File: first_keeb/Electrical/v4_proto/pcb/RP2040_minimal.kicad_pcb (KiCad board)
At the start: 2 copper layers, 80 x 80 mm, 64 parts, among them P1 USB4105-GF-A, Q1 SN74LV1T34DBV, SW1 SW_Push, SW2 SW_Push, SW3 SKRKAGE020, U1 NCP1117-3.3_SOT223, U2 LM4040DBZ-3, U3 PRTR5V0U2X, U4 W25Q32JVSS, U5 RP2040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

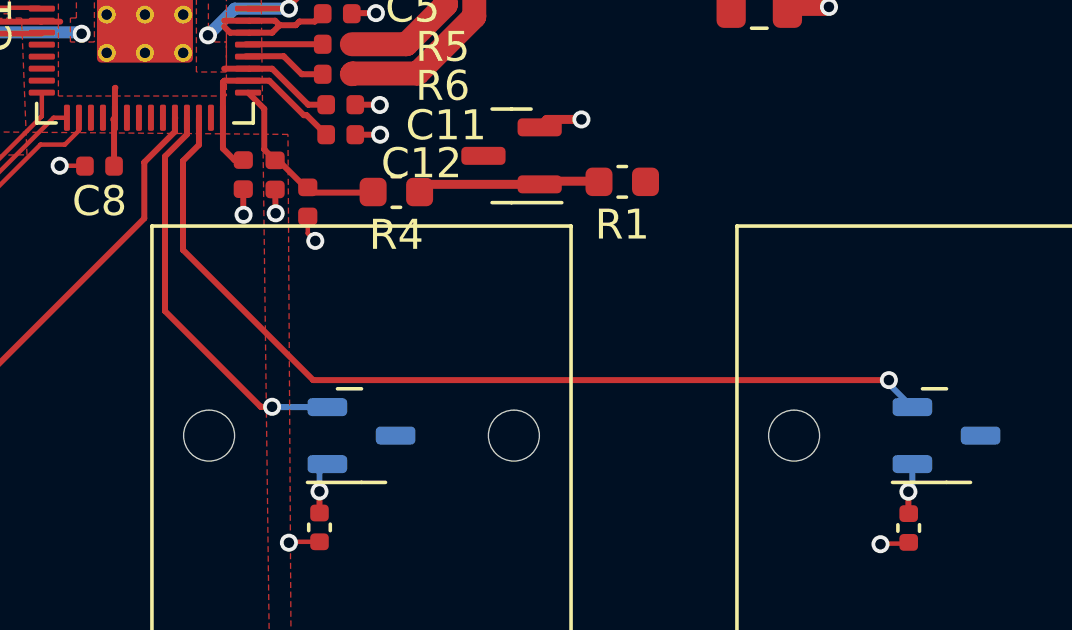
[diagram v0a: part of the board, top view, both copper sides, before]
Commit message: removes extra led
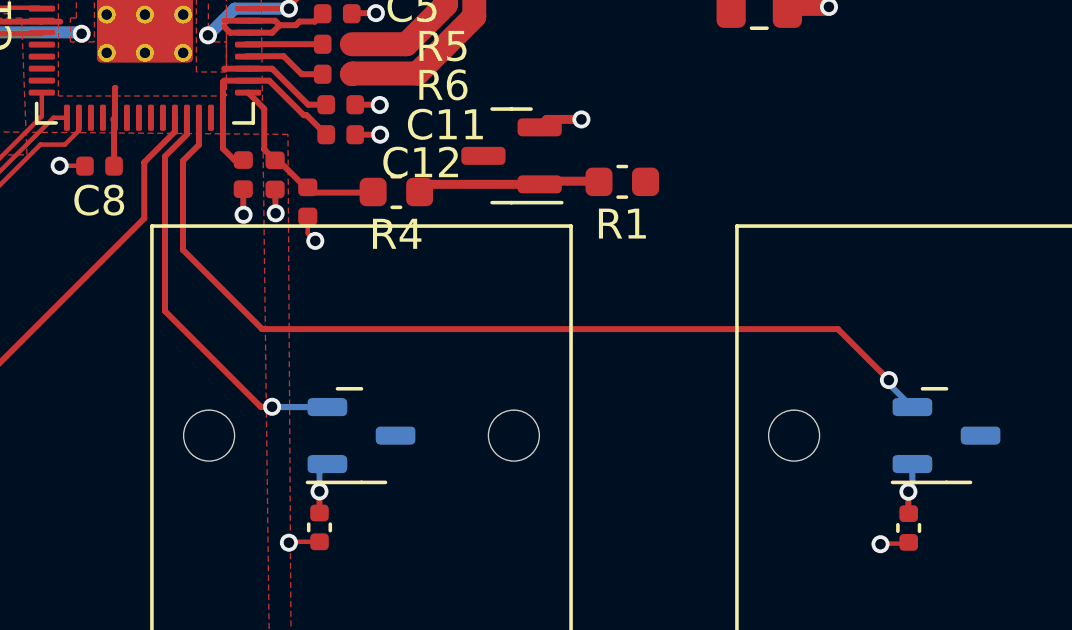
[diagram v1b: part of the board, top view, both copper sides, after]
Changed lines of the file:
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@@
   (segment (start 97.11 99.05) (end 98.8625 99.05) (width 0.2) (layer "B.Cu") (net 46))
   (segment (start 97.02 99.04) (end 97.11 99.05) (width 0.2) (layer "B.Cu") (net 46))
+  (segment (start 96.69 96.45) (end 94.05 93.81) (width 0.2) (layer "F.Cu") (net 47))
   (segment (start 94.579338 89.4075) (end 94.581838 89.405) (width 0.2) (layer "F.Cu") (net 47))
-  (segment (start 98.39 98.15) (end 94.05 93.81) (width 0.2) (layer "F.Cu") (net 47))
+  (segment (start 115.88 96.45) (end 96.69 96.45) (width 0.2) (layer "F.Cu") (net 47))
+  (segment (start 94.581838 90.308162) (end 94.581838 89.405) (width 0.2) (layer "F.Cu") (net 47))
   (segment (start 94.05 90.84) (end 94.581838 90.308162) (width 0.2) (layer "F.Cu") (net 47))
   (segment (start 94.05 93.81) (end 94.05 90.84) (width 0.2) (layer "F.Cu") (net 47))
-  (segment (start 117.58 98.15) (end 98.39 98.15) (width 0.2) (layer "F.Cu") (net 47))
-  (segment (start 94.581838 90.308162) (end 94.581838 89.405) (width 0.2) (layer "F.Cu") (net 47))
+  (segment (start 117.58 98.15) (end 115.88 96.45) (width 0.2) (layer "F.Cu") (net 47))
   (via (at 117.58 98.15) (size 0.6) (drill 0.35) (layers "F.Cu" "B.Cu") (net 47))
   (segment (start 117.58 98.28) (end 117.58 98.15) (width 0.15) (layer "B.Cu") (net 47))

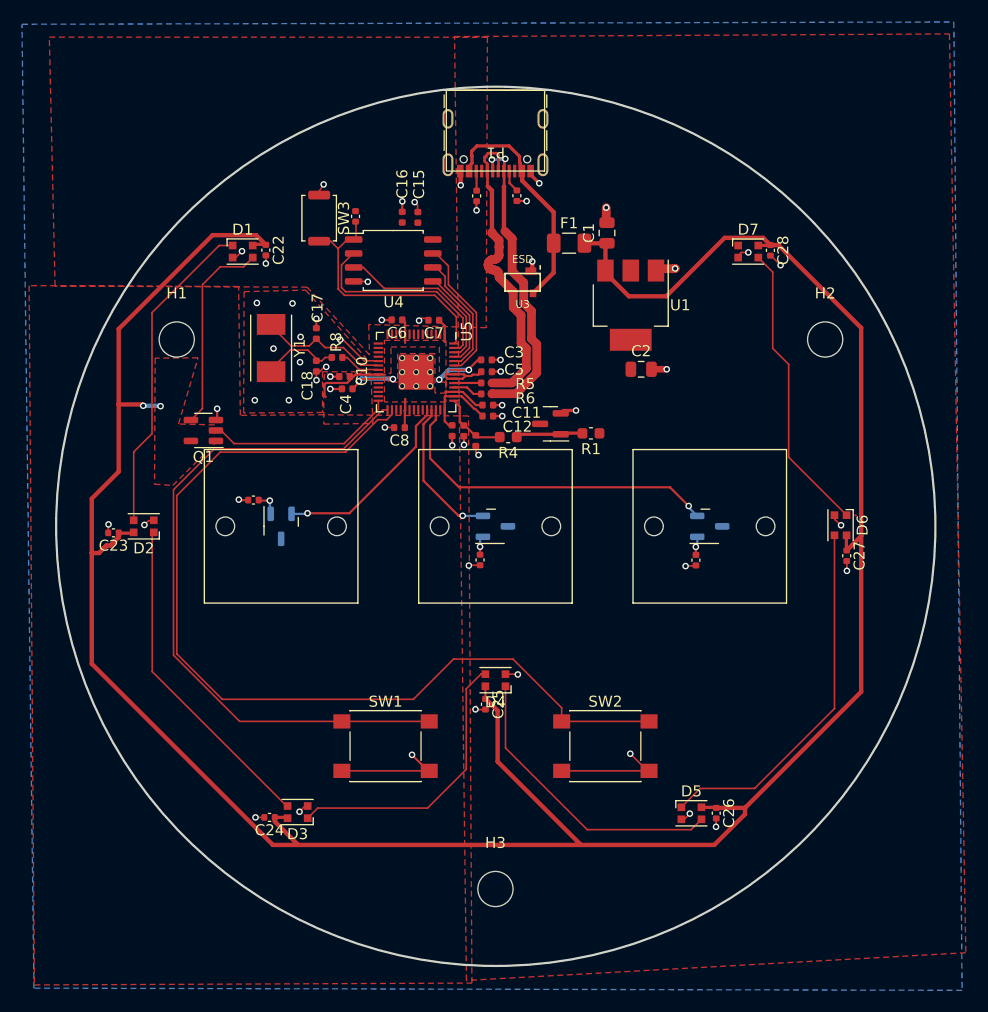
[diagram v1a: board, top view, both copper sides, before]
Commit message: makes 3v3 pour have more access
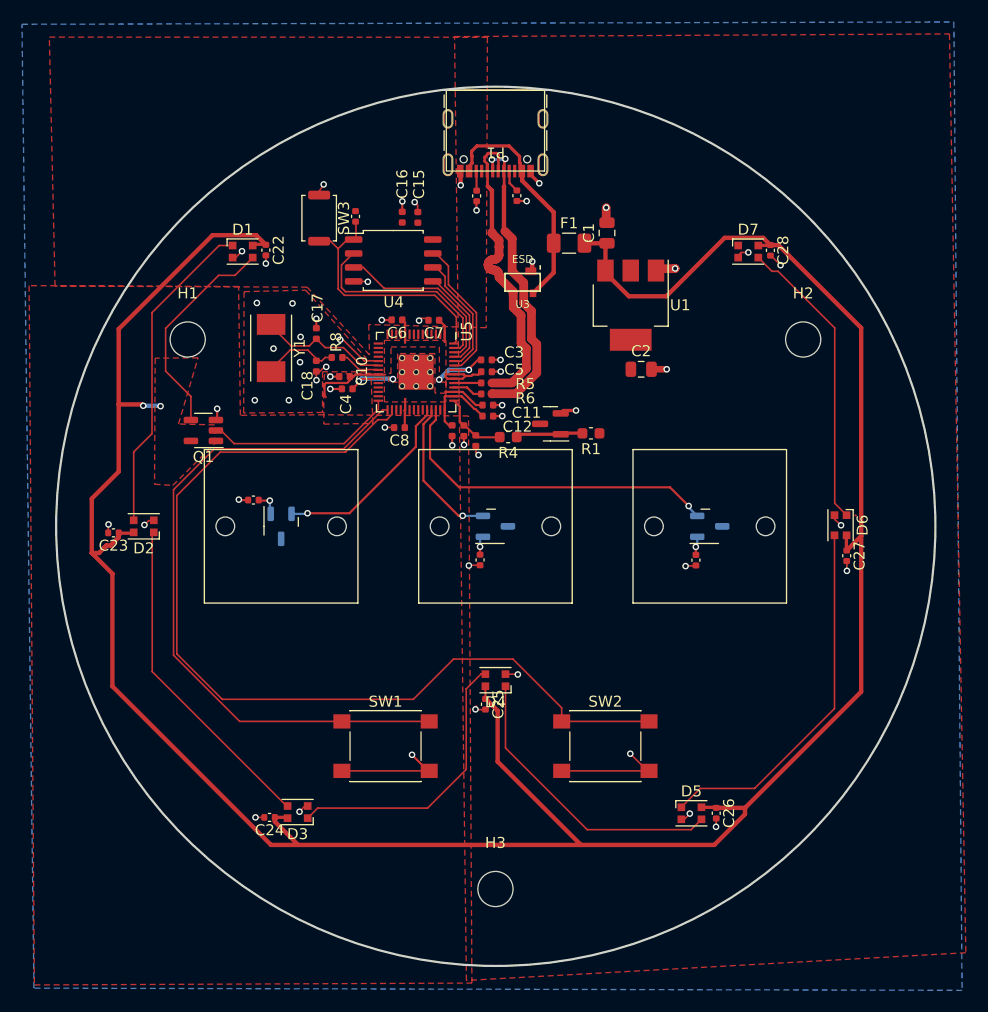
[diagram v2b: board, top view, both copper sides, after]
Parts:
- moved H2 2.00 mm to (128.0, 83.0)
- moved H1 1.00 mm to (72.0, 83.0)
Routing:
- net LED_D_5V: track 18.3 -> 19.9 mm
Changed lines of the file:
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@@
   )
   (footprint "MountingHole:MountingHole_3.2mm_M3" (layer "F.Cu")
-    (at 130 83)
+    (at 128 83)
     (descr "Mounting Hole 3.2mm, no annular, M3")
     (tags "mounting hole 3.2mm no annular m3")
@@
   )
   (footprint "MountingHole:MountingHole_3.2mm_M3" (layer "F.Cu")
-    (at 71 83)
+    (at 72 83)
     (descr "Mounting Hole 3.2mm, no annular, M3")
     (tags "mounting hole 3.2mm no annular m3")
@@
     )
   )
+  (gr_circle (center 100 100) (end 136 100)
+    (stroke (width 0.1) (type default)) (fill none) (layer "Cmts.User"))
   (gr_circle (center 100.029338 100) (end 60.029338 100)
     (stroke (width 0.2) (type default)) (fill none) (layer "Edge.Cuts"))
@@
   (segment (start 87.556838 86.8025) (end 87.799338 86.56) (width 0.4) (layer "B.Cu") (net 6))
   (segment (start 87.799338 86.56) (end 90.614368 86.56) (width 0.4) (layer "B.Cu") (net 6))
-  (segment (start 126.68 93.715) (end 126.68 85.26) (width 0.15) (layer "F.Cu") (net 10))
-  (segment (start 125.23 83.81) (end 125.23 76.865) (width 0.15) (layer "F.Cu") (net 10))
-  (segment (start 131.95 98.985) (end 126.68 93.715) (width 0.15) (layer "F.Cu") (net 10))
-  (segment (start 125.23 76.865) (end 123.915 75.55) (width 0.15) (layer "F.Cu") (net 10))
-  (segment (start 126.68 85.26) (end 125.23 83.81) (width 0.15) (layer "F.Cu") (net 10))
+  (segment (start 131.95 98.985) (end 130.87 97.905) (width 0.15) (layer "F.Cu") (net 10))
+  (segment (start 125.1625 76.7975) (end 123.915 75.55) (width 0.15) (layer "F.Cu") (net 10))
+  (segment (start 125.7175 76.7975) (end 125.1625 76.7975) (width 0.15) (layer "F.Cu") (net 10))
+  (segment (start 130.87 81.95) (end 125.7175 76.7975) (width 0.15) (layer "F.Cu") (net 10))
+  (segment (start 130.87 97.905) (end 130.87 81.95) (width 0.15) (layer "F.Cu") (net 10))
   (segment (start 132.82 99.03) (end 132.73 98.98) (width 0.15) (layer "F.Cu") (net 10))
   (segment (start 96.219338 83.3675) (end 96.439338 83.1475) (width 0.15) (layer "F.Cu") (net 18))
@@
   (segment (start 83.704319 84.9385) (end 83.704319 84.741) (width 0.15) (layer "F.Cu") (net 33))
   (segment (start 82.933319 83.97) (end 81.320356 83.97) (width 0.15) (layer "F.Cu") (net 33))
-  (segment (start 77.075 76.39) (end 77.915 75.55) (width 0.15) (layer "F.Cu") (net 37))
-  (segment (start 73.34 78.01) (end 74.96 76.39) (width 0.15) (layer "F.Cu") (net 37))
-  (segment (start 73.34 89.281838) (end 73.34 78.01) (width 0.15) (layer "F.Cu") (net 37))
-  (segment (start 72.291838 90.33) (end 73.34 89.281838) (width 0.15) (layer "F.Cu") (net 37))
-  (segment (start 74.96 76.39) (end 77.075 76.39) (width 0.15) (layer "F.Cu") (net 37))
+  (segment (start 74.815 77.165) (end 76.3 77.165) (width 0.15) (layer "F.Cu") (net 37))
+  (segment (start 69.99 85.88) (end 69.99 81.99) (width 0.15) (layer "F.Cu") (net 37))
+  (segment (start 72.291838 90.33) (end 72.291838 88.181838) (width 0.15) (layer "F.Cu") (net 37))
+  (segment (start 69.99 81.99) (end 74.815 77.165) (width 0.15) (layer "F.Cu") (net 37))
+  (segment (start 76.3 77.165) (end 77.915 75.55) (width 0.15) (layer "F.Cu") (net 37))
+  (segment (start 72.291838 88.181838) (end 69.99 85.88) (width 0.15) (layer "F.Cu") (net 37))
   (segment (start 77.915 74.45) (end 78.025 74.34) (width 0.3) (layer "F.Cu") (net 38))
   (segment (start 108.131838 74.2475) (end 110.149338 74.2475) (width 0.4) (layer "F.Cu") (net 38))
@@
   (segment (start 133.27701 81.941989) (end 133.27701 100.88299) (width 0.4) (layer "F.Cu") (net 38))
   (segment (start 65.72 88.91) (end 65.72 82.05) (width 0.4) (layer "F.Cu") (net 38))
+  (segment (start 65.15 114.56) (end 65.15 104.31) (width 0.4) (layer "F.Cu") (net 38))
   (segment (start 124.36 73.75) (end 120.86 73.75) (width 0.4) (layer "F.Cu") (net 38))
   (segment (start 63.27 102.43) (end 63.932964 102.43) (width 0.4) (layer "F.Cu") (net 38))
@@
   (segment (start 82.05 128.99) (end 79.9275 126.8675) (width 0.4) (layer "F.Cu") (net 38))
   (segment (start 99.085 114.55) (end 99.085 115.705) (width 0.2) (layer "F.Cu") (net 38))
-  (segment (start 63.27 112.506739) (end 63.27 102.43) (width 0.4) (layer "F.Cu") (net 38))
   (segment (start 67.83 88.91) (end 67.95 89.03) (width 0.4) (layer "F.Cu") (net 38))
   (segment (start 99.085 115.705) (end 99.09 115.71) (width 0.2) (layer "F.Cu") (net 38))
   (segment (start 81.22 126.48) (end 79.885 126.48) (width 0.3) (layer "F.Cu") (net 38))
   (segment (start 65.72 82.05) (end 74.26 73.51) (width 0.4) (layer "F.Cu") (net 38))
+  (segment (start 65.15 104.31) (end 63.27 102.43) (width 0.4) (layer "F.Cu") (net 38))
   (segment (start 99.132965 115.71) (end 99.09 115.71) (width 0.4) (layer "F.Cu") (net 38))
   (segment (start 110.360588 74.24) (end 110.01 74.590588) (width 0.4) (layer "F.Cu") (net 38))
   (segment (start 78.025 74.34) (end 79.255 74.34) (width 0.3) (layer "F.Cu") (net 38))
   (segment (start 107.78 128.99) (end 82.05 128.99) (width 0.4) (layer "F.Cu") (net 38))
-  (segment (start 82.05 128.99) (end 79.753261 128.99) (width 0.4) (layer "F.Cu") (net 38))
   (segment (start 67.06 100.625) (end 65.725 100.625) (width 0.3) (layer "F.Cu") (net 38))
-  (segment (start 79.753261 128.99) (end 63.27 112.506739) (width 0.4) (layer "F.Cu") (net 38))
   (segment (start 63.932964 102.43) (end 64.621482 101.741482) (width 0.4) (layer "F.Cu") (net 38))
   (segment (start 122.709239 125.62) (end 122.709239 126.190761) (width 0.4) (layer "F.Cu") (net 38))
@@
   (segment (start 110.01 74.590588) (end 110.01 76.73) (width 0.4) (layer "F.Cu") (net 38))
   (segment (start 112.139706 79.07) (end 110 76.930294) (width 0.4) (layer "F.Cu") (net 38))
+  (segment (start 79.58 128.99) (end 65.15 114.56) (width 0.4) (layer "F.Cu") (net 38))
   (segment (start 65.72 88.91) (end 67.83 88.91) (width 0.4) (layer "F.Cu") (net 38))
   (segment (start 115.54 79.07) (end 112.139706 79.07) (width 0.4) (layer "F.Cu") (net 38))
+  (segment (start 82.05 128.99) (end 79.58 128.99) (width 0.4) (layer "F.Cu") (net 38))
   (segment (start 133.27701 100.88299) (end 131.96 102.2) (width 0.4) (layer "F.Cu") (net 38))
   (segment (start 108.024338 74.355) (end 108.131838 74.2475) (width 0.4) (layer "F.Cu") (net 38))

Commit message: first prototype of case
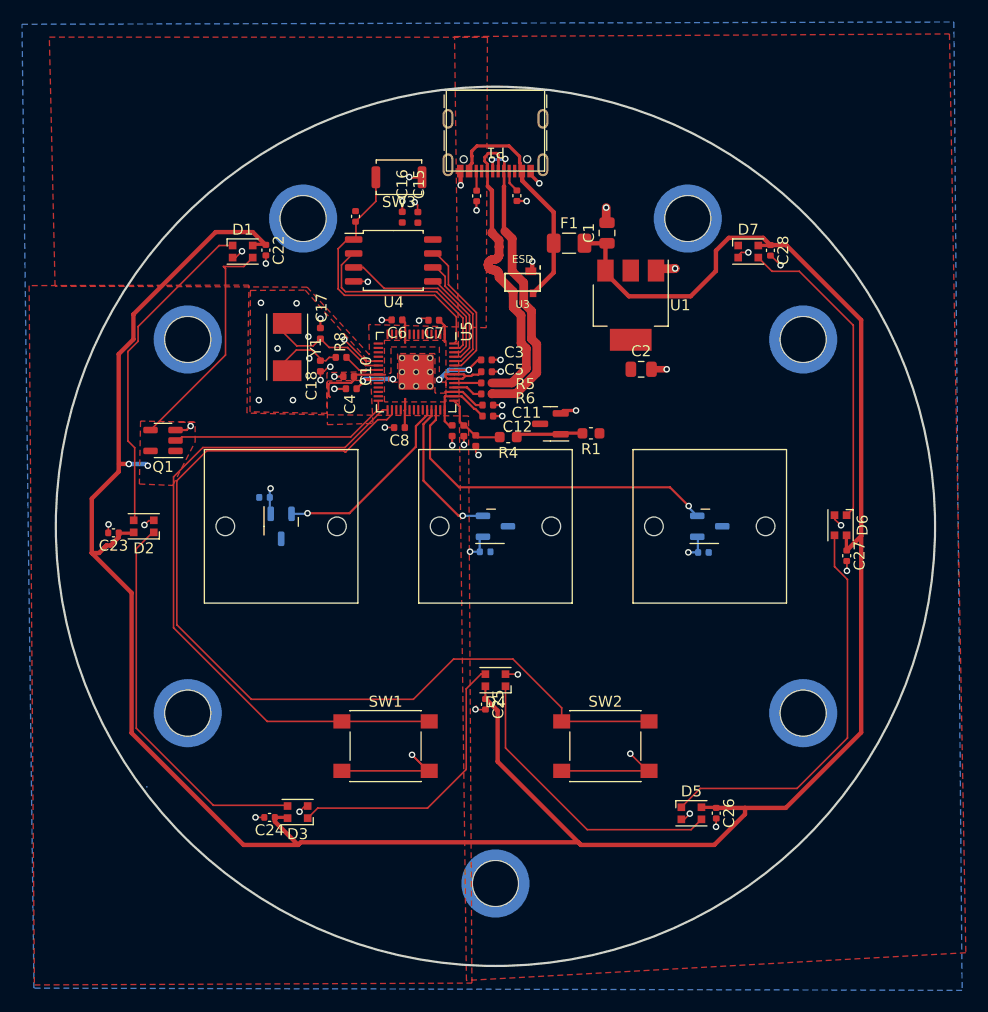
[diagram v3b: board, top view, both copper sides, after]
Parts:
- removed the C20 at (98.6, 103.1)
- removed C21: 1u, Capacitor_SMD:C_0402_1005Metric
- added C20: 1u, Capacitor_SMD:C_0402_1005Metric, B.Cu at (118.9, 102.4)
- added C20: 1u, Capacitor_SMD:C_0402_1005Metric, B.Cu at (99.1, 102.3)
- added H3: M3_Threaded_Insert, MountingHole:M3_Threaded_Insert, B.Cu at (117.5, 72.0)
- added H4: M3_Threaded_Insert, MountingHole:M3_Threaded_Insert, B.Cu at (128.0, 117.0)
- added H6: M3_Threaded_Insert, MountingHole:M3_Threaded_Insert, B.Cu at (72.0, 117.0)
- added H7: M3_Threaded_Insert, MountingHole:M3_Threaded_Insert, B.Cu at (82.5, 72.0)
- C19: moved to B.Cu
- H1, H2: value MountingHole_3.2mm_M3 -> M3_Threaded_Insert; footprint MountingHole:MountingHole_3.2mm_M3 -> MountingHole:M3_Threaded_Insert; moved to B.Cu
- H5: renamed from H3; value MountingHole_3.2mm_M3 -> M3_Threaded_Insert; footprint MountingHole:MountingHole_3.2mm_M3 -> MountingHole:M3_Threaded_Insert; moved to B.Cu
- moved H1 56.0 mm to (128.0, 83.0), turned to 180 degrees
- moved H2 56.0 mm to (72.0, 83.0), turned to 180 degrees
- moved SW3 8.16 mm to (91.2, 68.2), turned to 180 degrees
- moved Q1 3.79 mm to (69.8, 92.2)
- moved Y1 1.46 mm to (81.0, 83.7)
- moved C19 1.04 mm to (79.0, 97.4)
- moved H5 0.50 mm to (100.0, 132.5), turned to 180 degrees
- moved C17 0.37 mm to (84.1, 82.4)
- moved C18 0.37 mm to (84.1, 85.4)
- moved C10 0.37 mm to (86.6, 86.4)
- moved C4 0.37 mm to (86.9, 87.5)
- moved R8 0.37 mm to (86.0, 84.6)
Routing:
- net Net-(D2-DOUT): track 30.1 -> 35.1 mm
- net +5V: track 241.5 -> 245.9 mm
- net Net-(D5-DOUT): track 33.4 -> 36.7 mm
- net GND: track 72.3 -> 69.1 mm, vias 56 -> 53
- net GPIO17: track 17.4 -> 20.4 mm
- net /QSPI_SS: track 23.3 -> 26.1 mm
- net +3V3: track 33.3 -> 34.9 mm
- net Net-(D6-DOUT): track 27.2 -> 28.7 mm
- net LED_D_5V: track 19.9 -> 20.8 mm
- net GPIO18: track 63.3 -> 62.5 mm
- net +1V1: track 16.0 -> 15.3 mm
- net GPIO19: track 86.8 -> 86.2 mm
- net Net-(D1-DOUT): track 29.8 -> 30.3 mm
